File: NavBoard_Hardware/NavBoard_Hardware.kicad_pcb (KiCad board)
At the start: 2 copper layers, 61 x 100 mm, 60 parts, among them J1 Conn_Coaxial, Q1 BSS138, Q2 BSS138, U2 ATMEGA328P-Project_Library, U3 OKI, U4 OKI, U5 FGPMMOPA6H, Y1 Crystal

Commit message: Added dates and what not
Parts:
- moved G*** 0.90 mm to (127.6, 139.7)
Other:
- board text added: "Attend ONE Onboarding meeting in"
- board text added: "Austin Christman (accxd4@mst.edu)"
- board text added: "Brian Dahlman (bcdz6c@mst.edu),"
- board text added: "EMAN103; 8PM; AUG 28, 29"
- board text added: "Learn Design PCBs in THREE sessions"
- board text added: "Location TBD; 2-4pm; Sat. Sept. 7, 14, 21"
- board text added: "Questions? Contact Marsrover@mst.edu,"
- board text added: "Zak Brooks (zkbnv3@mst.edu), or"
- board text removed: "DAY 1 -- Saturday, September 7"
- board text removed: "DAY 2 -- Saturday, September 13"
- board text removed: "DAY 3 -- Saturday, September 20"
- board text removed: "Learn to create your very own PCB!"
- board text removed: "Navigation Board, Rev2 Mars Rover Design Team Missouri S&T, 2019"
- board text removed: "Onboarding meeting this week -- Mon/Wed/Fri"
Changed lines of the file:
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@@
   (general
     (thickness 1.6)
-    (drawings 76)
+    (drawings 78)
     (tracks 508)
     (zones 0)
@@
   )
   (module MRDT_Silkscreens:MRDT_Logo_20mm (layer F.Cu)
-    (at 127.762 138.811)
+    (at 127.635 139.7)
     (tags "Logo, MRDT")
     (fp_text reference G*** (at -3.6068 11.8364) (layer Dwgs.User) hide
@@
     )
   )
-  (gr_text "Onboarding meeting this week -- Mon/Wed/Fri" (at 146.05 132.08) (layer B.SilkS)
-    (effects (font (size 1.5 1.5) (thickness 0.3)) (justify mirror))
+  (gr_text "Zak Brooks (zkbnv3@mst.edu), or" (at 153.035 147.955) (layer F.SilkS)
+    (effects (font (size 1.27 1.27) (thickness 0.3)))
   )
-  (gr_text "DAY 3 -- Saturday, September 20" (at 152.4 149.225) (layer B.SilkS)
-    (effects (font (size 1.5 1.5) (thickness 0.3)) (justify mirror))
+  (gr_text "Austin Christman (accxd4@mst.edu)" (at 153.035 149.86) (layer F.SilkS)
+    (effects (font (size 1.27 1.27) (thickness 0.3)))
   )
-  (gr_text "DAY 2 -- Saturday, September 13" (at 152.4 146.05) (layer B.SilkS)
-    (effects (font (size 1.5 1.5) (thickness 0.3)) (justify mirror))
+  (gr_text "Brian Dahlman (bcdz6c@mst.edu), \n" (at 153.035 146.05) (layer F.SilkS)
+    (effects (font (size 1.27 1.27) (thickness 0.3)))
   )
-  (gr_text "DAY 1 -- Saturday, September 7" (at 153.035 142.875) (layer B.SilkS)
-    (effects (font (size 1.5 1.5) (thickness 0.3)) (justify mirror))
+  (gr_text "Questions? Contact Marsrover@mst.edu,\n" (at 151.765 143.51) (layer F.SilkS)
+    (effects (font (size 1.27 1.27) (thickness 0.3)))
+  )
+  (gr_text "Location TBD; 2-4pm; Sat. Sept. 7, 14, 21\n" (at 153.035 139.7) (layer F.SilkS)
+    (effects (font (size 1.27 1.27) (thickness 0.3)))
   )
-  (gr_text "Learn to create your very own PCB! " (at 144.78 139.7) (layer B.SilkS)
-    (effects (font (size 2.032 2.032) (thickness 0.3)) (justify mirror))
+  (gr_text "EMAN103; 8PM; AUG 28, 29 " (at 154.94 134.62) (layer F.SilkS)
+    (effects (font (size 1.5 1.5) (thickness 0.3)))
+  )
+  (gr_text "Attend ONE Onboarding meeting in " (at 155.575 132.08) (layer F.SilkS)
+    (effects (font (size 1.5 1.5) (thickness 0.3)))
+  )
+  (gr_text "Learn Design PCBs in THREE sessions " (at 153.67 137.795) (layer F.SilkS)
+    (effects (font (size 1.27 1.27) (thickness 0.3)))
   )
   (gr_text "MRDT E-PCB SUBTEAM" (at 144.78 71.12) (layer B.SilkS)
@@
   (gr_line (start 119.3292 70.485) (end 119.3292 70.231) (layer F.SilkS) (width 0.2))
   (gr_line (start 119.3292 76.454) (end 119.3292 70.485) (layer F.SilkS) (width 0.2))
-  (gr_text "Navigation Board, Rev2\nMars Rover Design Team\nMissouri S&T, 2019\n" (at 154.8638 139.7) (layer F.SilkS)
-    (effects (font (size 1.5 1.5) (thickness 0.3)))
-  )
   (segment (start 117.0432 86.614) (end 117.0432 86.5886) (width 0.381) (layer F.Cu) (net 1))
   (segment (start 119.120096 123.195904) (end 119.0752 123.2408) (width 0.381) (layer B.Cu) (net 1))

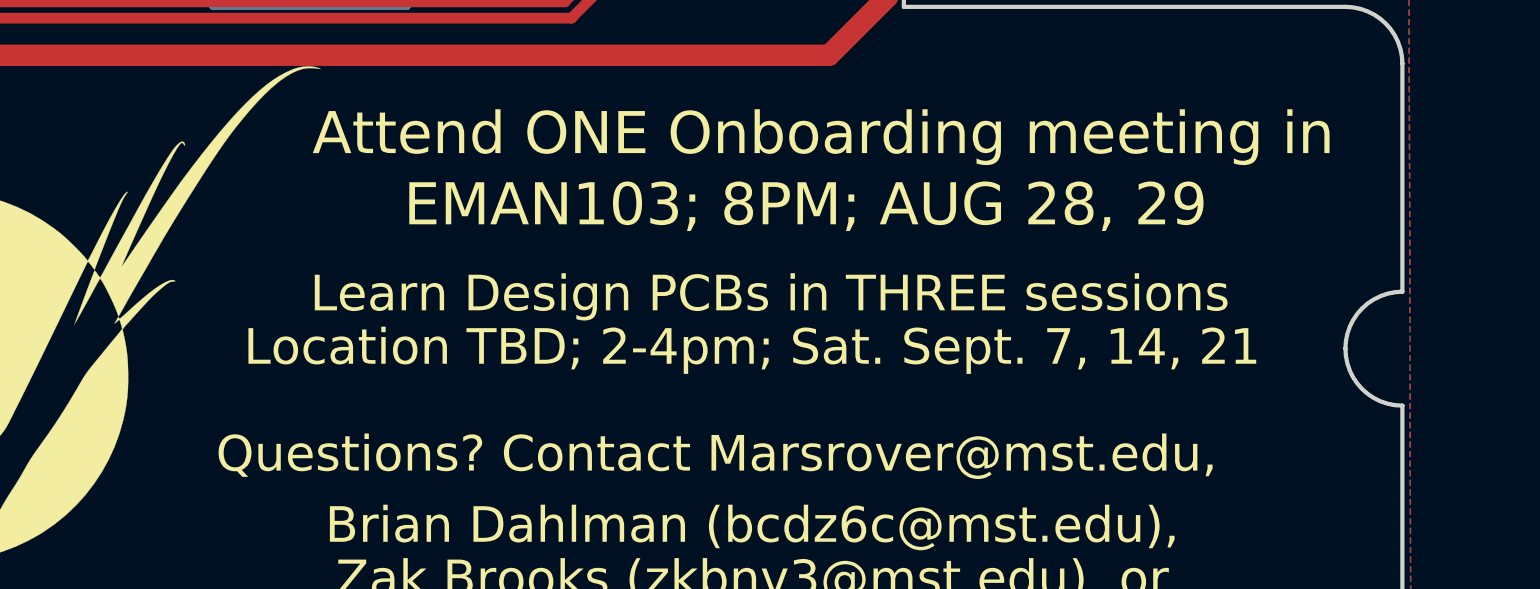
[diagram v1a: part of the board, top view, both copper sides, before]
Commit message: Readjusted silk screen
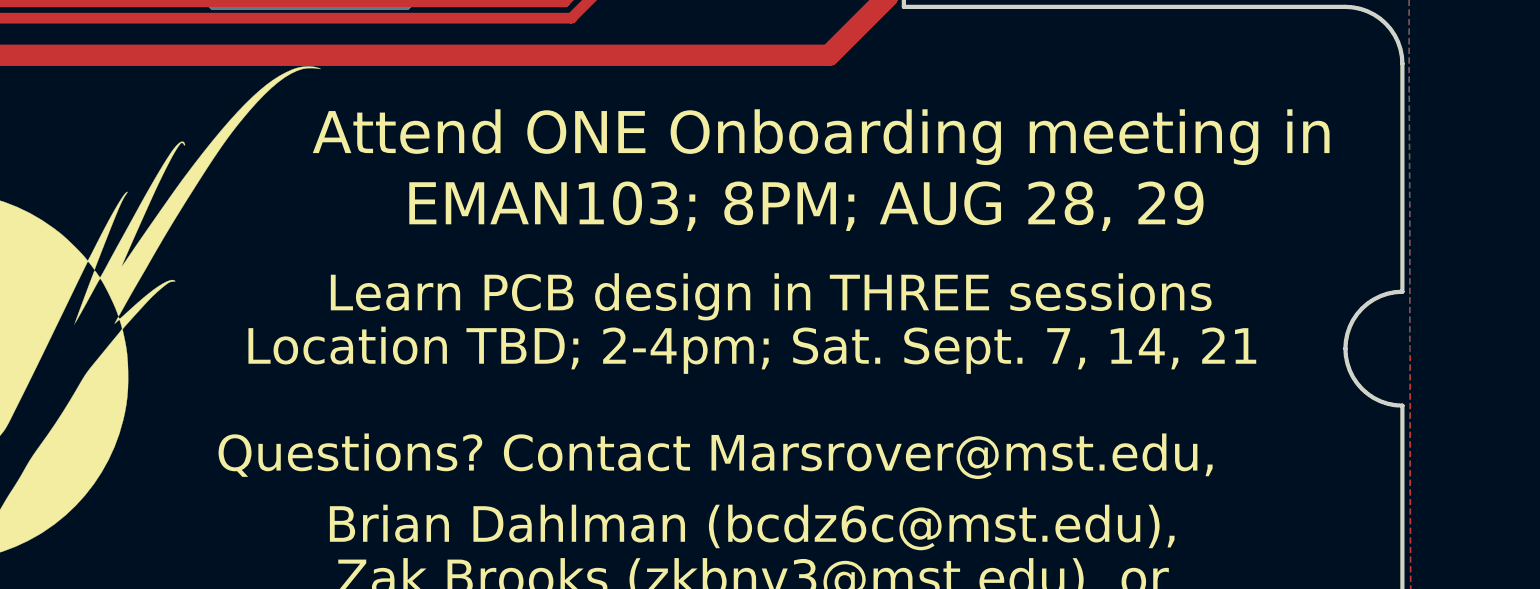
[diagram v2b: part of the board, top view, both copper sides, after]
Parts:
- added G***: LOGO, MRDT_Silkscreens:zz_Valkyrie_Logo_Full_58.4mmx76mm, B.Cu at (146.1, 113.7)
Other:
- board text added: "#ROVESOHARD"
- board text added: "Learn PCB design in THREE sessions"
- board text added: "MARS ROVER DESIGN TEAM"
- board text added: "TODAY. TOMORROW. FOREVER."
- board text removed: "3 2 1"
- board text removed: "4 3 2 1"
- board text removed: "GND"
- board text removed: "IMU_RX"
- board text removed: "Learn Design PCBs in THREE sessions"
- board text removed: "MRDT E-PCB SUBTEAM"
- board text removed: "PRGM_RX"
- board text removed: "PRGM_TX"
- board text removed: "RESET"
- board text removed: "SCL"
- board text removed: "SDA"
